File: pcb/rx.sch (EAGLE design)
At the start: 30 parts, among them J1 USB_A_PTH_MALE, Y1 CRYSTAL-26MHZSMD-3.2X2.5

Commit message: added holes to button
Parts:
- U$10: value 324_SW -> 324_SW324_SWITCH_FOOT_HOLE; device 3pos_slide_switch:324_SW -> 3pos_slide_switch:324_SW324_SWITCH_FOOT_HOLE
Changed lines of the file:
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@@
 <part name="SJ1" library="SparkFun-Jumpers" deviceset="JUMPER-SMT_2_NC_TRACE" device="_NO-SILK"/>
 <part name="+3V6" library="supply1" library_urn="urn:adsk.eagle:library:371" deviceset="+3V3" device=""/>
-<part name="U$10" library="3pos_slide_switch" deviceset="324_SW" device=""/>
+<part name="U$10" library="3pos_slide_switch" deviceset="324_SW" device="324_SWITCH_FOOT_HOLE" value="324_SW324_SWITCH_FOOT_HOLE"/>
 <part name="LED2" library="joyAnalog" deviceset="LED" device="CHIP-LED0805"/>
 <part name="GND22" library="supply1" library_urn="urn:adsk.eagle:library:371" deviceset="GND" device=""/>

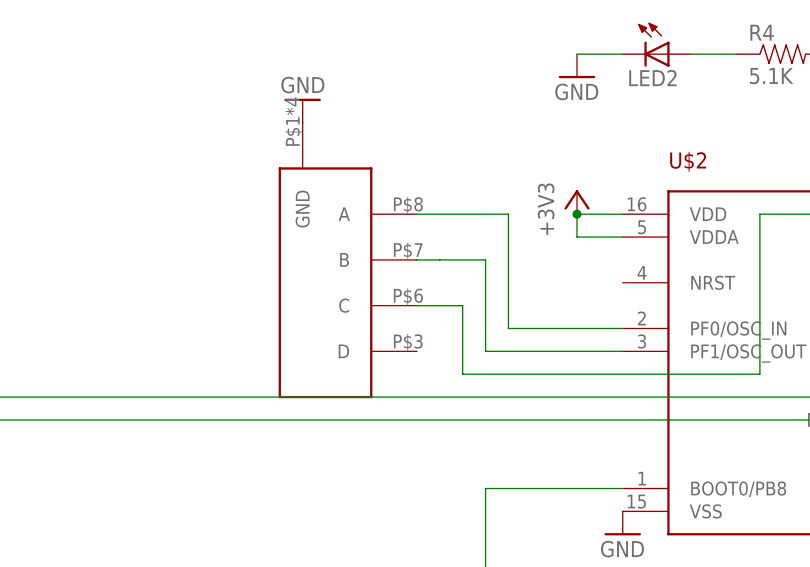
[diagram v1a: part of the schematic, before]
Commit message: updated PCB, firmware sleep working
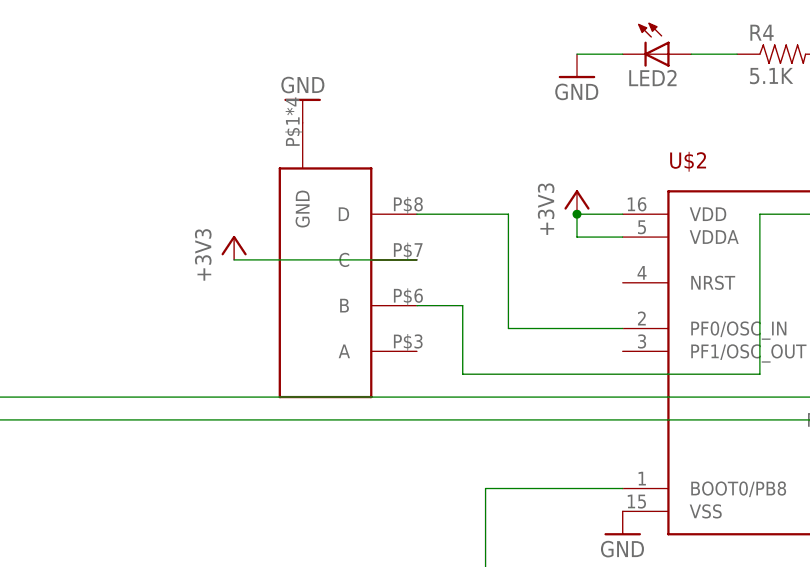
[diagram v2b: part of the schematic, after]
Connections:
- removed net N$25: U$1.B, U$2.PF1/OSC_OUT
- net +3V3: now also U$1.C
- net N$10: now also U$1.D; no longer U$1.A
- net N$26: now also U$1.B; no longer U$1.C
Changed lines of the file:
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@@
 <part name="GND23" library="supply1" library_urn="urn:adsk.eagle:library:371" deviceset="GND" device=""/>
 <part name="U$5" library="adafruit_changed" deviceset="PINHD5" device=""/>
+<part name="+3V5" library="supply1" library_urn="urn:adsk.eagle:library:371" deviceset="+3V3" device=""/>
 </parts>
 <sheets>
@@
 <instance part="GND23" gate="1" x="71.12" y="-12.7"/>
 <instance part="U$5" gate="G$1" x="81.28" y="-7.62"/>
+<instance part="+3V5" gate="G$1" x="-30.48" y="22.86"/>
 </instances>
 <busses>
@@
 <pinref part="U$5" gate="G$1" pin="4"/>
 </segment>
+<segment>
+<pinref part="+3V5" gate="G$1" pin="+3V3"/>
+<pinref part="U$1" gate="G$1" pin="C"/>
+<wire x1="-30.48" y1="20.32" x2="-10.16" y2="20.32" width="0.1524" layer="91"/>
+</segment>
 </net>
 <net name="N$1" class="0">
@@
 <wire x1="12.7" y1="12.7" x2="0" y2="12.7" width="0.1524" layer="91"/>
 <wire x1="0" y1="12.7" x2="0" y2="25.4" width="0.1524" layer="91"/>
-<pinref part="U$1" gate="G$1" pin="A"/>
+<pinref part="U$1" gate="G$1" pin="D"/>
 <wire x1="0" y1="25.4" x2="-10.16" y2="25.4" width="0.1524" layer="91"/>
-</segment>
-</net>
-<net name="N$25" class="0">
-<segment>
-<pinref part="U$2" gate="G$1" pin="PF1/OSC_OUT"/>
-<wire x1="12.7" y1="10.16" x2="-2.54" y2="10.16" width="0.1524" layer="91"/>
-<wire x1="-2.54" y1="10.16" x2="-2.54" y2="20.32" width="0.1524" layer="91"/>
-<wire x1="-2.54" y1="20.32" x2="-7.62" y2="20.32" width="0.1524" layer="91"/>
-<pinref part="U$1" gate="G$1" pin="B"/>
-<wire x1="-7.62" y1="20.32" x2="-10.16" y2="20.32" width="0.1524" layer="91"/>
 </segment>
 </net>
@@
 <wire x1="27.94" y1="7.62" x2="-5.08" y2="7.62" width="0.1524" layer="91"/>
 <wire x1="-5.08" y1="7.62" x2="-5.08" y2="15.24" width="0.1524" layer="91"/>
-<pinref part="U$1" gate="G$1" pin="C"/>
+<pinref part="U$1" gate="G$1" pin="B"/>
 <wire x1="-5.08" y1="15.24" x2="-10.16" y2="15.24" width="0.1524" layer="91"/>
 </segment>
